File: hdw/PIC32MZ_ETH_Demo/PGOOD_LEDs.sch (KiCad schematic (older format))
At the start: 10 parts

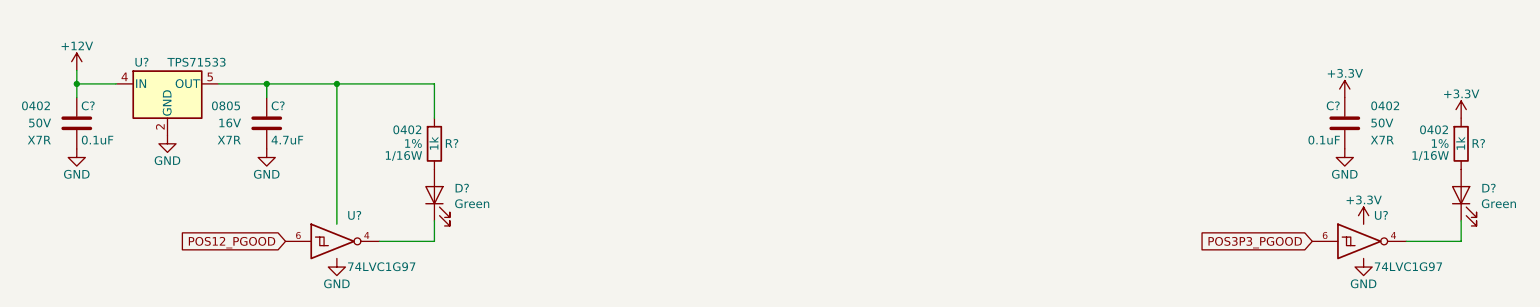
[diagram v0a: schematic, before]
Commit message: More schematic tweaks, followed PHY design guide
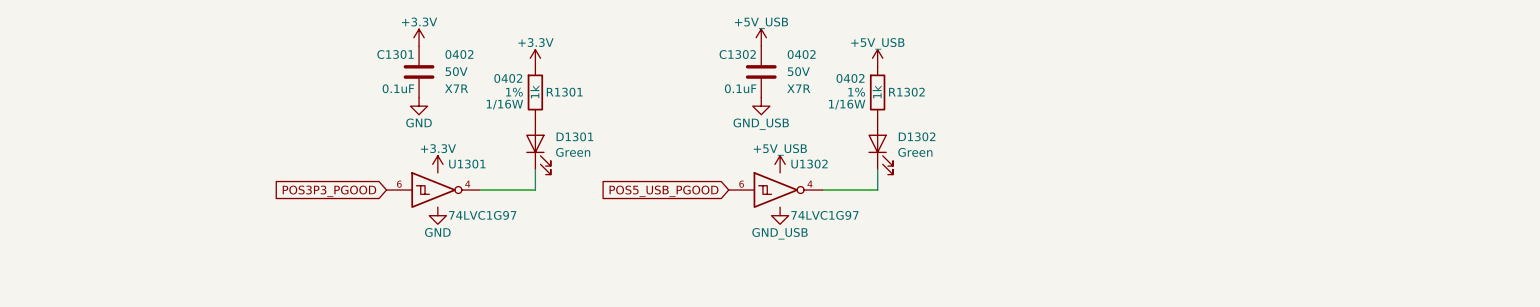
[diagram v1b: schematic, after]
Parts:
- removed C?: 0.1uF, Capacitors_SMD:C_0402, symbol Custom_Library:C_Custom
- removed C?: 4.7uF, Capacitors_SMD:C_0805, symbol Custom_Library:C_Custom
- removed D?: Green, LEDs:LED_0603, symbol Device:LED
- removed R?: 1k, Resistors_SMD:R_0402, symbol Custom_Library:R_Custom
- removed U?: 74LVC1G97, Package_TO_SOT_SMD:SOT-363_SC-70-6, symbol Custom_Library:74LVC1G97_Power_NOT
- removed U?: TPS71533, Package_TO_SOT_SMD:SOT-353_SC-70-5, symbol Regulator_Linear:TPS71533__SC70
- added C1302: 0.1uF, Capacitors_SMD:C_0402, symbol Custom_Library:C_Custom
- added D1302: Green, LEDs:LED_0603, symbol Device:LED
- added R1302: 1k, Resistors_SMD:R_0402, symbol Custom_Library:R_Custom
- added U1302: 74LVC1G97, Package_TO_SOT_SMD:SOT-363_SC-70-6, symbol Custom_Library:74LVC1G97_Power_NOT
- gave numbers to parts that had none: 4
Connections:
- new net: D1302.1 (K), U1302.4
- new net: D1302.2 (A), R1302.2
- new net +5V_USB: C1302.1, R1302.1, U1302.1 (VCC), U1302.5 (VCC)
- new net GND_USB: C1302.2, U1302.2 (GND), U1302.3 (GND)
- new net POS5_USB_PGOOD: U1302.6
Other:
- moved on the sheet: C1301, D1301, R1301, U1301

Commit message: Populated digi-key pn's
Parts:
- C1301, C1302: Digi-Key PN (none) -> 490-10701-1-ND
- D1301, D1302: footprint LEDs:LED_0603 -> LEDs:LED_0402; Digi-Key PN (none) -> 1497-1219-1-ND
- R1301, R1302: Digi-Key PN (none) -> 541-1.00KLCT-ND
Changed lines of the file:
@@
 F 2 "Capacitors_SMD:C_0402" H 3498 1730 50  0001 C CNN
 F 3 "" H 3485 1980 50  0001 C CNN
-F 4 "" H 3885 2380 60  0001 C CNN "Digi-Key PN"
+F 4 "490-10701-1-ND" H 3885 2380 60  0001 C CNN "Digi-Key PN"
 F 5 "0402" H 3310 1980 50  0000 R CNN "display_footprint"
 F 6 "50V" H 3310 1880 50  0000 R CNN "Voltage"
@@
 F 0 "D1301" V 4179 2183 50  0000 R CNN
 F 1 "Green" V 4088 2183 50  0000 R CNN
-F 2 "LEDs:LED_0603" H 4140 2300 50  0001 C CNN
+F 2 "LEDs:LED_0402" H 4140 2300 50  0001 C CNN
 F 3 "~" H 4140 2300 50  0001 C CNN
-F 4 "" H -1020 -4020 50  0001 C CNN "Digi-Key PN"
+F 4 "1497-1219-1-ND" H -1020 -4020 50  0001 C CNN "Digi-Key PN"
 	1    4140 2300
 	0    -1   -1   0
@@
 F 5 "1%" H 4210 2000 50  0000 L CNN "Tolerance"
 F 6 "1/16W" H 4210 1930 50  0000 L CNN "Wattage"
-F 7 "" H 4440 2400 60  0001 C CNN "Digi-Key PN"
+F 7 "541-1.00KLCT-ND" H 4440 2400 60  0001 C CNN "Digi-Key PN"
 	1    4140 2000
 	-1   0    0    -1
@@
 F 2 "Capacitors_SMD:C_0402" H 5498 1730 50  0001 C CNN
 F 3 "" H 5485 1980 50  0001 C CNN
-F 4 "" H 5885 2380 60  0001 C CNN "Digi-Key PN"
+F 4 "490-10701-1-ND" H 5885 2380 60  0001 C CNN "Digi-Key PN"
 F 5 "0402" H 5310 1980 50  0000 R CNN "display_footprint"
 F 6 "50V" H 5310 1880 50  0000 R CNN "Voltage"
@@
 F 0 "D1302" V 6179 2183 50  0000 R CNN
 F 1 "Green" V 6088 2183 50  0000 R CNN
-F 2 "LEDs:LED_0603" H 6140 2300 50  0001 C CNN
+F 2 "LEDs:LED_0402" H 6140 2300 50  0001 C CNN
 F 3 "~" H 6140 2300 50  0001 C CNN
-F 4 "" H 980 -4020 50  0001 C CNN "Digi-Key PN"
+F 4 "1497-1219-1-ND" H 980 -4020 50  0001 C CNN "Digi-Key PN"
 	1    6140 2300
 	0    -1   -1   0
@@
 F 5 "1%" H 6210 2000 50  0000 L CNN "Tolerance"
 F 6 "1/16W" H 6210 1930 50  0000 L CNN "Wattage"
-F 7 "" H 6440 2400 60  0001 C CNN "Digi-Key PN"
+F 7 "541-1.00KLCT-ND" H 6440 2400 60  0001 C CNN "Digi-Key PN"
 	1    6140 2000
 	-1   0    0    -1
